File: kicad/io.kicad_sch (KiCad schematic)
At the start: 20 parts, among them J1 Conn_01x01, J4 Conn_01x08, J5 Conn_01x02, J7 Conn_01x08, J8 Conn_01x02, J9 Conn_01x02, U38 74HC74

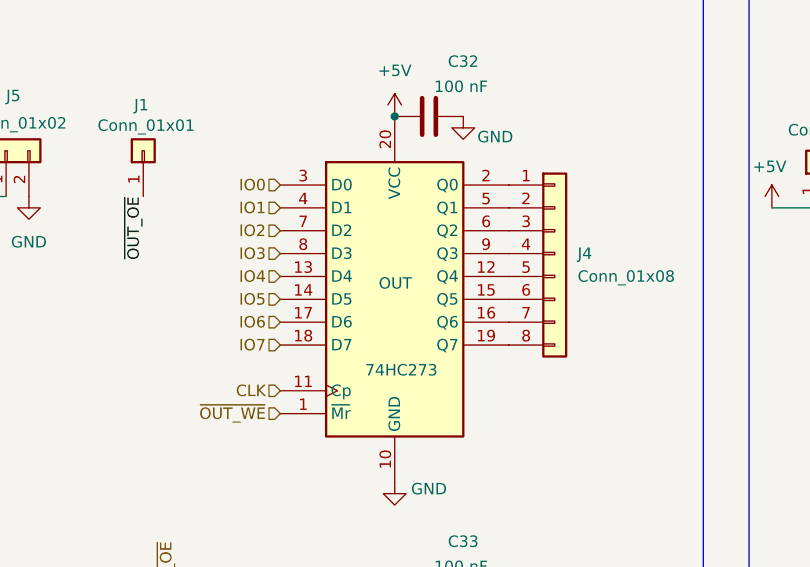
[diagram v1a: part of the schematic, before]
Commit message: kicad: compact design
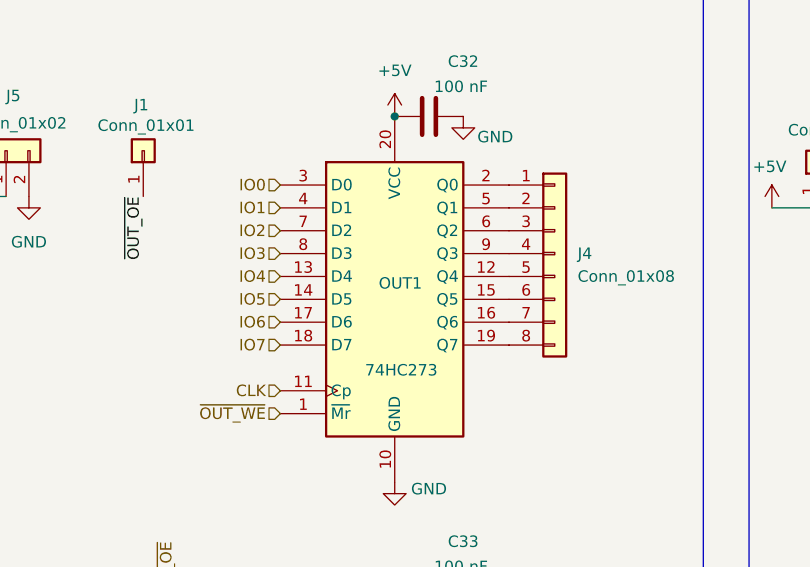
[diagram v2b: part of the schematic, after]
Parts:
- renumbered OUT to OUT1
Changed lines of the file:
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@@
 		(on_board yes)
 		(dnp no)
-		(property "Reference" "OUT"
+		(property "Reference" "OUT1"
 			(at 104.902 65.532 0)
 			(effects
@@
 			(project "SC08v2"
 				(path "/8273a279-6d4f-43cc-a94b-c590a7d8a356/37fe5901-445c-47a7-bd1d-3cc6d41d9e81"
-					(reference "OUT")
+					(reference "OUT1")
 					(unit 1)
 				)

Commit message: kicad: finalize sketch
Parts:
- removed INP_FLAG0, OUT_FLAG0, U38: 74HC74, symbol 74xx:74HC74
- added IODFLIPFLOP_U1: 74HC74, Package_DIP:DIP-14_W7.62mm, symbol 74xx:74HC74
- INPFLAG_U1: renamed from INP_FLAG1; footprint (none) -> Package_DIP:DIP-20_W7.62mm
- INPFLAG_U_C1: renamed from C30; footprint (none) -> Capacitor_THT:C_Disc_D3.0mm_W1.6mm_P2.50mm
- INP_CONN0: renamed from J8; footprint (none) -> Connector_PinHeader_2.54mm:PinHeader_1x02_P2.54mm_Vertical
- INP_CONN1: renamed from J9; footprint (none) -> Connector_PinHeader_2.54mm:PinHeader_1x02_P2.54mm_Vertical
- INP_CONN2: renamed from J7; footprint (none) -> Connector_PinHeader_2.54mm:PinHeader_1x08_P2.54mm_Vertical
- INP_U0_C1: renamed from C29; footprint (none) -> Capacitor_THT:C_Disc_D3.0mm_W1.6mm_P2.50mm
- INP_U1: renamed from INP1; footprint (none) -> Package_DIP:DIP-20_W7.62mm
- INP_U1_C1: renamed from C28; footprint (none) -> Capacitor_THT:C_Disc_D3.0mm_W1.6mm_P2.50mm
- IODFLIPFLOP_U_C1: renamed from C31; footprint (none) -> Capacitor_THT:C_Disc_D3.0mm_W1.6mm_P2.50mm
- OUT_CONN0: renamed from J5; footprint (none) -> Connector_PinHeader_2.54mm:PinHeader_1x02_P2.54mm_Vertical
- OUT_CONN1: renamed from J1; footprint (none) -> Connector_PinHeader_2.54mm:PinHeader_1x01_P2.54mm_Vertical
- OUT_CONN2: renamed from J4; footprint (none) -> Connector_PinHeader_2.54mm:PinHeader_1x08_P2.54mm_Vertical
- OUT_FLAG_U1: renamed from OUT_FLAG1; footprint (none) -> Package_DIP:DIP-20_W7.62mm
- OUT_FLAG_U_C1: renamed from C33; footprint (none) -> Capacitor_THT:C_Disc_D3.0mm_W1.6mm_P2.50mm
- OUT_U_C1: renamed from C32; footprint (none) -> Capacitor_THT:C_Disc_D3.0mm_W1.6mm_P2.50mm
- renumbered INP0 to INP_U0, OUT1 to OUT_U1
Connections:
- net +5V: now also IODFLIPFLOP_U1.14 (VCC)
- net GND: now also IODFLIPFLOP_U1.7 (GND)
- net ~{INP_OE}: now also IODFLIPFLOP_U1.13 (~{R})
- net ~{INP_WE}: now also IODFLIPFLOP_U1.10 (~{S})
- net ~{OUT_OE}: now also IODFLIPFLOP_U1.1 (~{R}), IODFLIPFLOP_U1.4 (~{S})
- net at INPFLAG_U1.2 (A0), INPFLAG_U1.3 (A1), INPFLAG_U1.4 (A2)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: now also IODFLIPFLOP_U1.9 (Q)
- net at OUT_FLAG_U1.2 (A0), OUT_FLAG_U1.3 (A1), OUT_FLAG_U1.4 (A2)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: now also IODFLIPFLOP_U1.5 (Q)
- no-connect marks 0 -> 6
